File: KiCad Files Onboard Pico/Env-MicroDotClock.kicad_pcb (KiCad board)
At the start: 2 copper layers, 110 x 80 mm, 87 parts, among them IC1 IS31FL3730-QFLS2-TR, IC2 IS31FL3730-QFLS2-TR, IC3 IS31FL3730-QFLS2-TR, IC4 IS31FL3730-QFLS2-TR, J1 Conn_01x03, J3 Button, M1 Dip-14 Socket, M2 Dip-14 Socket, M3 Dip-14 Socket, M4 Dip-14 Socket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

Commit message: commit current progress
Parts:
- added R10: 0402 10K, Resistor_SMD:R_0402_1005Metric, F.Cu at (35.9, 61.1)
- added R11: 0402 10K, Resistor_SMD:R_0402_1005Metric, F.Cu at (35.9, 59.0)
- added R12: 0402 10K, Resistor_SMD:R_0402_1005Metric, F.Cu at (35.9, 60.0)
- added R13: 0402 10K, Resistor_SMD:R_0402_1005Metric, F.Cu at (35.9, 58.0)
- added R28: 0402 10K, Resistor_SMD:R_0402_1005Metric, F.Cu at (35.9, 57.0)
- added R5: 0402 10K, Resistor_SMD:R_0402_1005Metric, F.Cu at (35.9, 52.9)
- added R6: 0402 10K, Resistor_SMD:R_0402_1005Metric, F.Cu at (35.9, 54.0)
- added R7: 0402 10K, Resistor_SMD:R_0402_1005Metric, F.Cu at (35.9, 55.0)
- added R8: 0402 10K, Resistor_SMD:R_0402_1005Metric, F.Cu at (35.9, 56.0)
- added R9: 0402 10K, Resistor_SMD:R_0402_1005Metric, F.Cu at (35.9, 62.1)
- moved J1 2.00 mm to (52.0, 54.2), turned to 90 degrees
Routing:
- net +3V3: track 218.5 -> 129.0 mm, vias 8 -> 7
- net GPIO6: track 40.9 -> 84.5 mm, vias 2 -> 4
- net GPIO7: track 40.5 -> 82.2 mm, vias 0 -> 2
- net GPIO8: track 25.4 -> 66.0 mm, vias 2 -> 4
- net GPIO9: track 23.1 -> 62.6 mm, vias 0 -> 2
- net GPIO10: track 14.8 -> 52.6 mm, vias 0 -> 2
- net GPIO11: track 17.6 -> 54.2 mm, vias 0 -> 2
- net GPIO14: track 41.3 -> 74.1 mm, vias 2 -> 4
- net GPIO13: track 24.8 -> 56.6 mm, vias 0 -> 2
- net GPIO15: track 40.3 -> 71.9 mm, vias 0 -> 2
- net GPIO12: track 26.4 -> 57.3 mm, vias 2 -> 4
- net Net-(BT1-+): track 60.6 -> 50.3 mm
- net SWCLK: track 16.0 -> 11.8 mm
- net GND: vias 25 -> 22

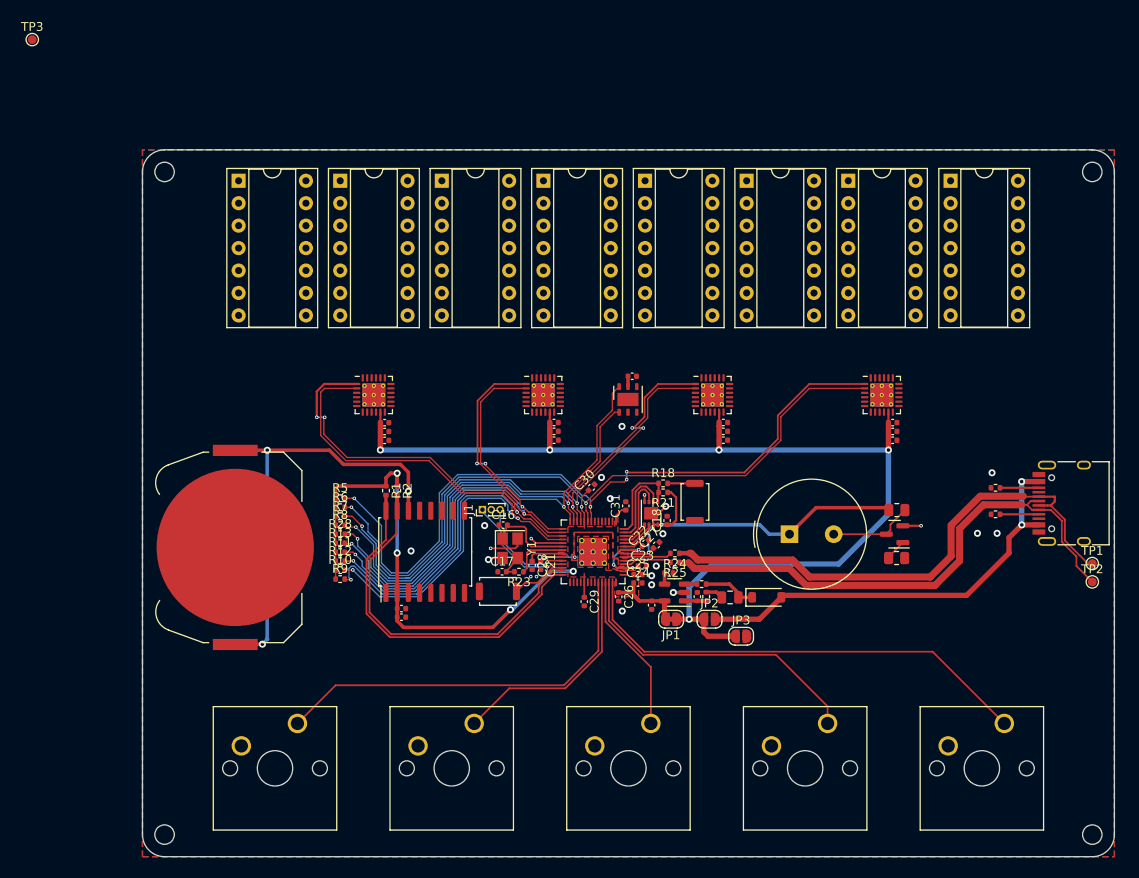
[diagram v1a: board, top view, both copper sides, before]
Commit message: finished up and cleaned up PCB, added logos
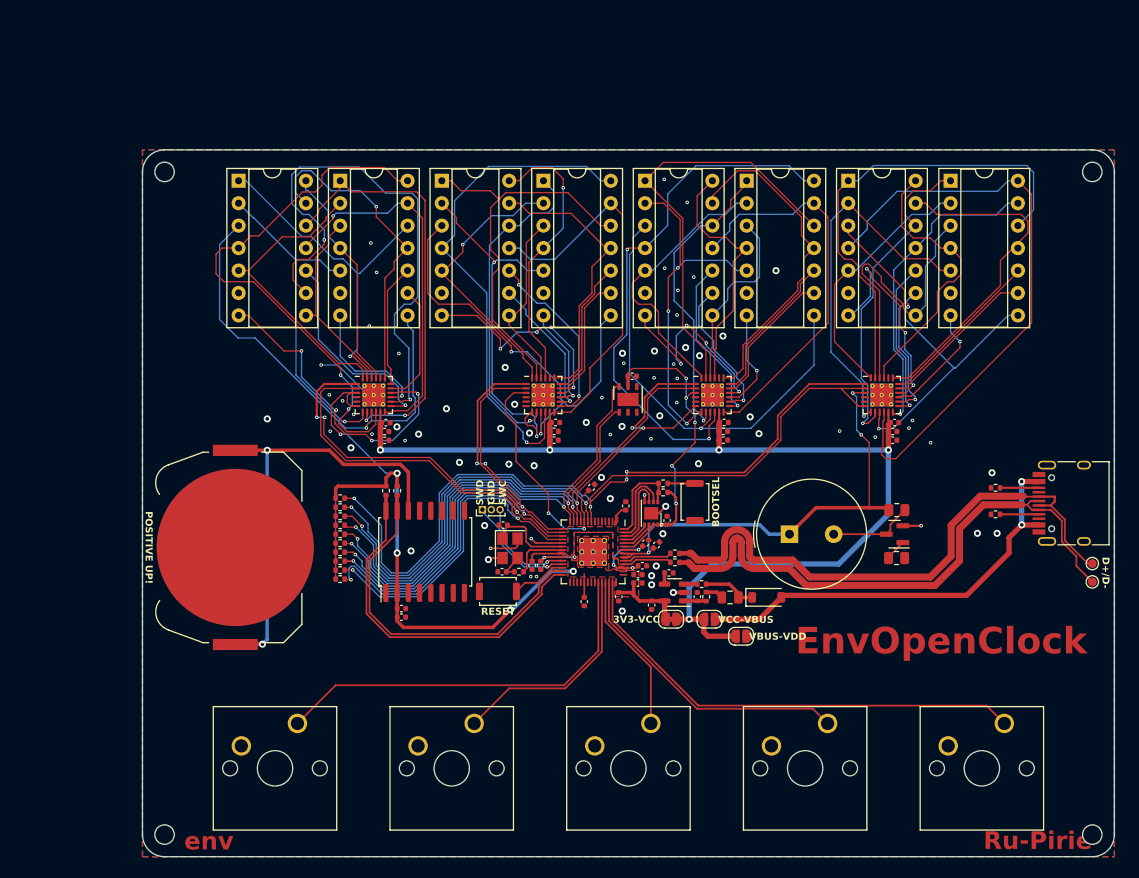
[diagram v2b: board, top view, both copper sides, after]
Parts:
- removed TP3: TestPoint, TestPoint:TestPoint_Pad_D1.0mm
- U2: value SOT-23-5 5.5V 3.3V 500mA -> TLV75733PDBVR
- moved C7 0.22 mm to (98.6, 44.4)
- moved C12 0.17 mm to (60.2, 44.4)
- moved C11 0.15 mm to (41.0, 44.4)
- moved C1 0.08 mm to (79.3, 44.4)
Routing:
- net +3V3: track 129.0 -> 208.2 mm, vias 7 -> 16
- net IC4R4: track 0.00 -> 68.0 mm
- net IC1R7: track 0.00 -> 61.5 mm, vias 0 -> 2
- net IC1R4: track 0.00 -> 61.5 mm, vias 0 -> 2
- net IC3R4: track 0.00 -> 60.1 mm, vias 0 -> 2
- net IC2R4: track 0.00 -> 57.2 mm, vias 0 -> 1
- net IC4C2: track 0.00 -> 53.7 mm
- net IC1R3: track 0.00 -> 53.0 mm, vias 0 -> 1
- net IC3R3: track 0.00 -> 51.8 mm, vias 0 -> 1
- net IC2R3: track 0.00 -> 50.6 mm, vias 0 -> 2
- net IC1R2: track 0.00 -> 48.3 mm, vias 0 -> 2
- net IC3C2: track 0.00 -> 48.1 mm
- net IC2C2: track 0.00 -> 45.2 mm
- net IC3R5: track 0.00 -> 44.3 mm
- net IC4R3: track 0.00 -> 44.2 mm, vias 0 -> 2
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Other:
- board text added: "3V3-VCC"
- board text added: "BOOTSEL"
- board text added: "D+/D-"
- board text added: "EnvOpenClock"
- board text added: "POSITIVE UP!"
- board text added: "RESET"
- board text added: "Ru-Pirie"
- board text added: "SWD GND SWC"
- board text added: "VBUS-VDD"
- board text added: "VCC-VBUS"
- board text added: "env"

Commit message: generated production files
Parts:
- added TP3: TestPoint, TestPoint:TestPoint_Pad_D1.0mm, F.Cu at (80.2, 52.0)
- H1, H2, H3, H4: value MountingHole -> M2
- J1: value Conn_01x03 -> 1mm 1x3
- SW1, SW2, SW3, SW4, SW5: value SW_Push -> MX Keyboard Switch
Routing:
- net /Onboard Pico/~{USB_BOOT}: track 3.09 -> 7.53 mm

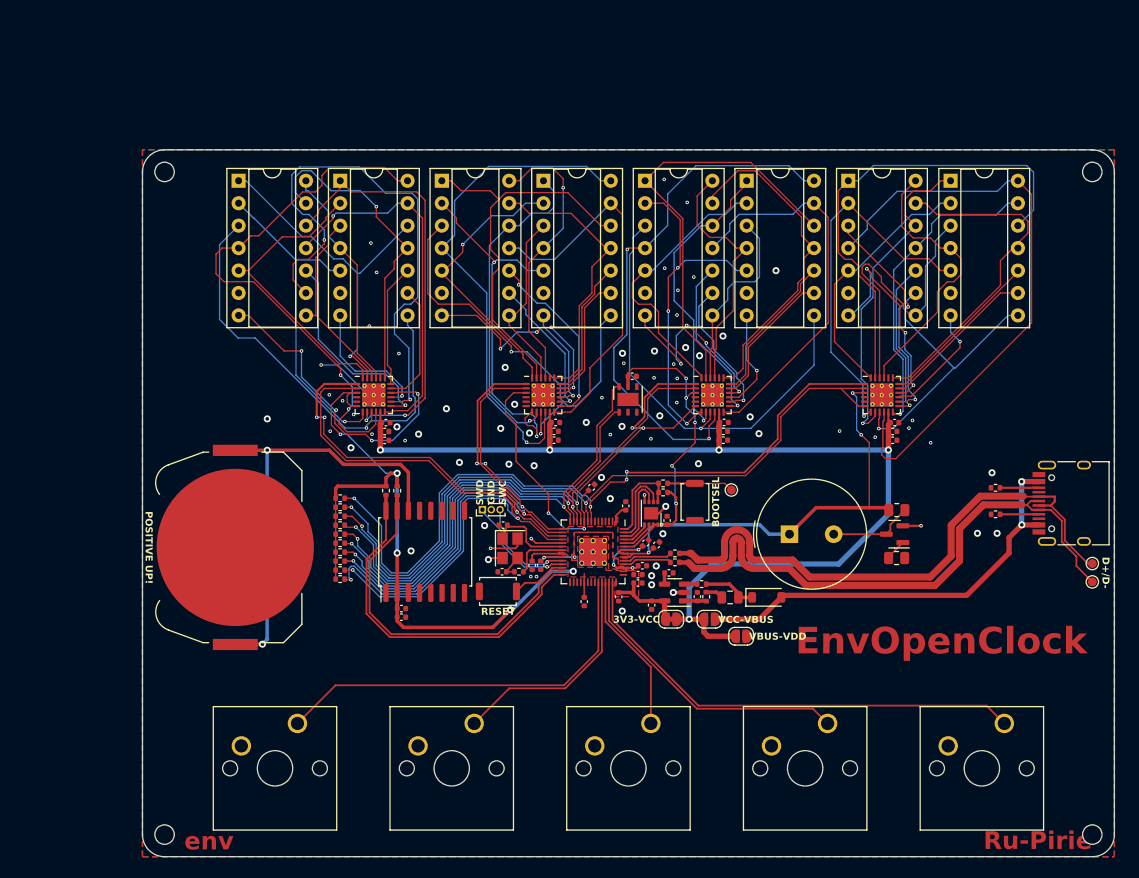
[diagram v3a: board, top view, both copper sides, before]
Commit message: added thermal vias, improved gnd connections from IS31FL37s, added thermal vias, added power only usb port on the back.
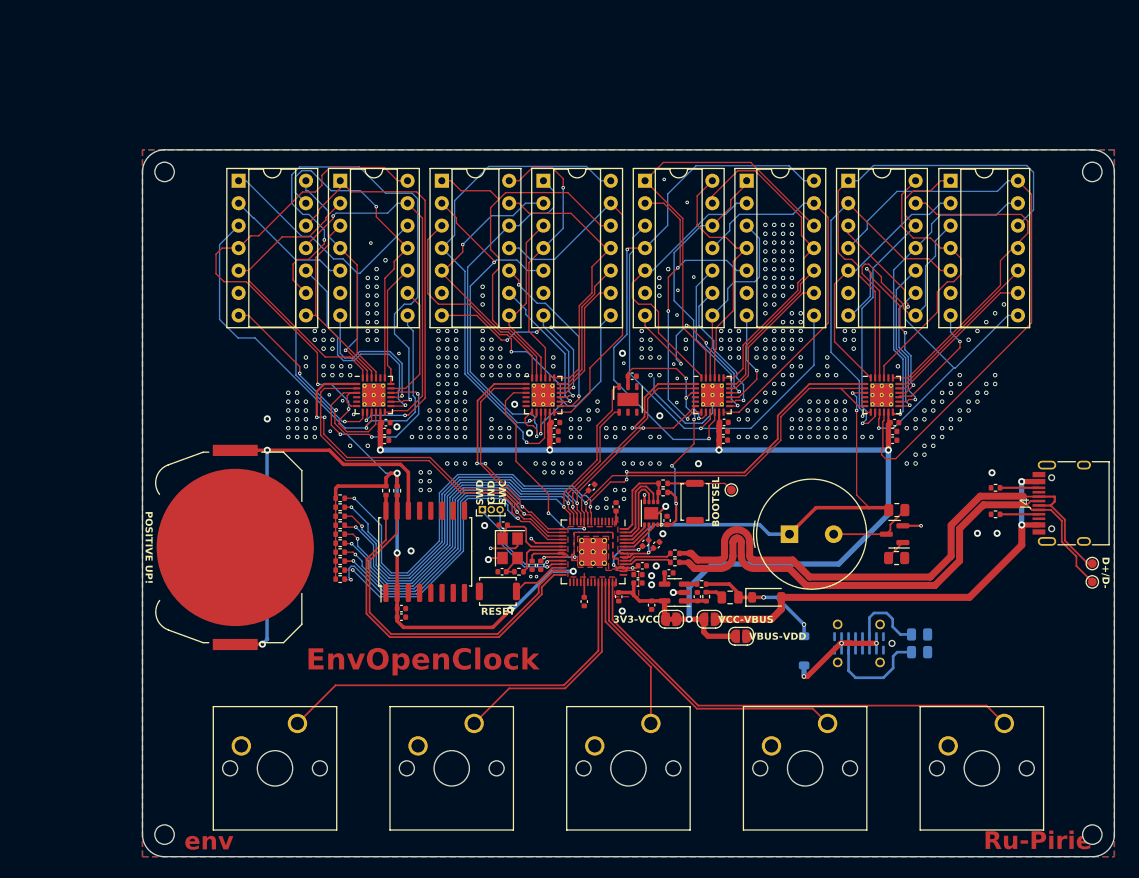
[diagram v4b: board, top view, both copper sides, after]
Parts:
- removed USB1: TYPE-C-31-M-12, Connector_USB:USB_C_Receptacle_HRO_TYPE-C-31-M-12
- added D2: 1N4002W, Diode_SMD:D_SOD-123, B.Cu at (88.4, 70.2)
- added J2: GT-USB-7051A, Connector_USB:USB_C_Receptacle_G-Switch_GT-USB-7051x, B.Cu at (94.6, 69.4)
- added J4: TYPE-C-31-M-12, Connector_USB:USB_C_Receptacle_HRO_TYPE-C-31-M-12, F.Cu at (119.0, 53.5)
- added R14: 5.1K 0805, Resistor_SMD:R_0805_2012Metric, B.Cu at (101.5, 68.3)
- added R17: 5.1K 0805, Resistor_SMD:R_0805_2012Metric, B.Cu at (101.5, 70.3)
- moved R15 3.00 mm to (110.0, 51.8)
- moved R16 3.00 mm to (110.0, 54.8)
- moved C31 1.10 mm to (67.1, 53.9)
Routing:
- net Net-(D2-A): track 0.00 -> 15.1 mm, vias 0 -> 3
- net Net-(J2-CC2): track 0.00 -> 11.8 mm
- net Net-(J2-CC1): track 0.00 -> 8.66 mm
- net VSYS: track 6.13 -> 14.6 mm, vias 0 -> 2
- net GND: track 24.4 -> 26.7 mm, vias 75 -> 423
- net IC2R2: track 36.9 -> 38.9 mm
- net IC2R1: track 42.8 -> 44.8 mm
- net IC1R6: track 23.8 -> 25.8 mm
- net IC1R8: track 15.4 -> 17.4 mm
- net IC1C8: track 35.8 -> 34.3 mm
- net IC2C8: track 25.2 -> 23.7 mm
- net VBUS: track 48.9 -> 50.0 mm
- net +3V3: track 208.2 -> 207.3 mm
- net IC3R1: track 40.1 -> 39.4 mm
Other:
- board text added: "PWR ONLY"

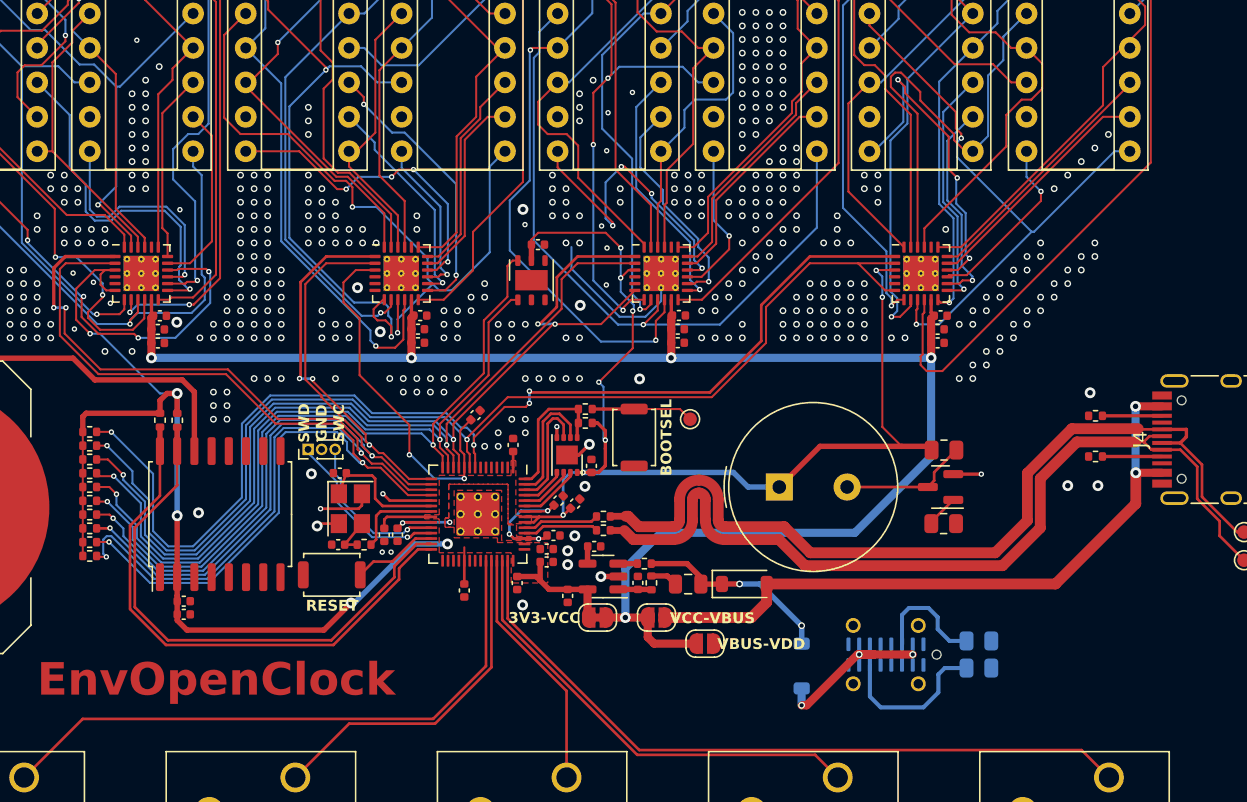
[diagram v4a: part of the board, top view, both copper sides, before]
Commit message: swapped LDO for more capable switching regulator.
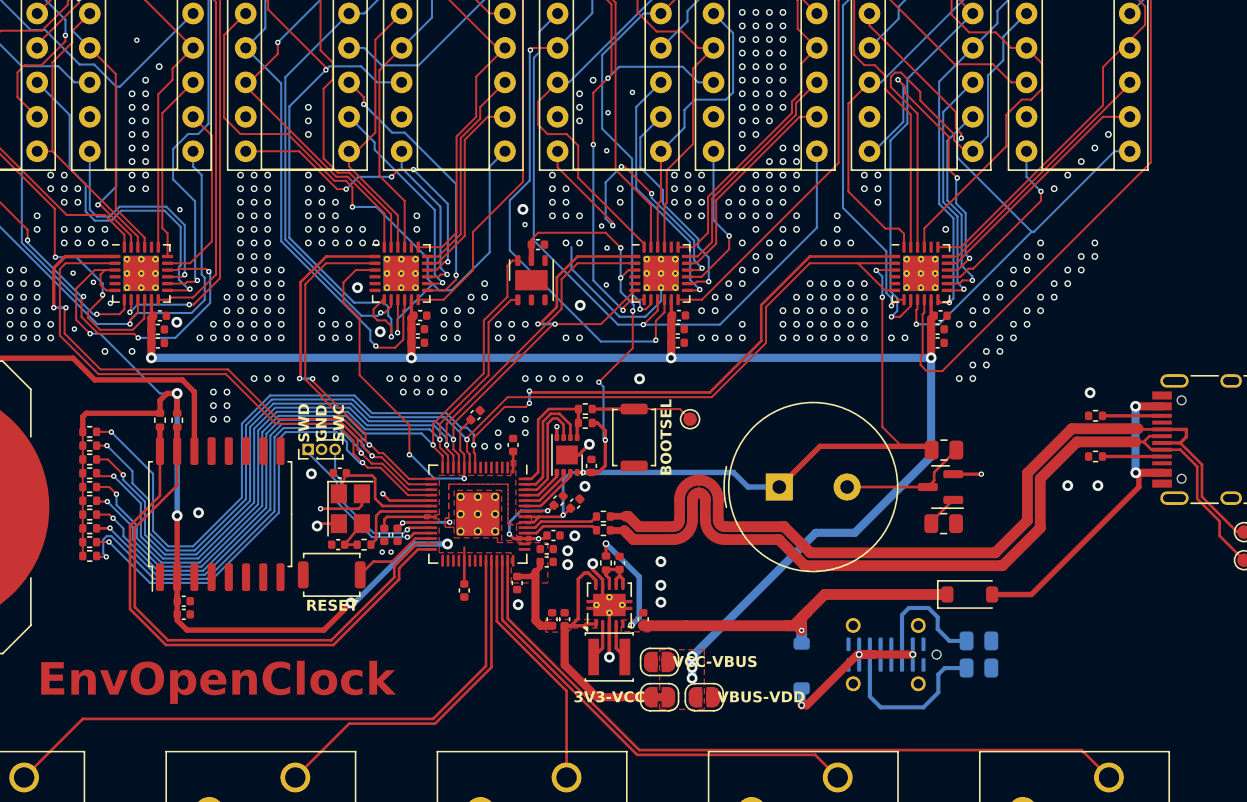
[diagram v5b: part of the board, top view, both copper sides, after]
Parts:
- removed CBP1: 10uf 0402, Capacitor_SMD:C_0402_1005Metric
- removed F1: 0805L050WR, Fuse:Fuse_0805_2012Metric
- removed FB1: FerriteBead 0402, Resistor_SMD:R_0402_1005Metric
- removed R22: 100K 0402, Resistor_SMD:R_0402_1005Metric
- added C15: 10uF 0402, Capacitor_SMD:C_0402_1005Metric, F.Cu at (76.7, 66.8)
- added C32: 10uF 0402, Capacitor_SMD:C_0402_1005Metric, F.Cu at (70.0, 66.8)
- added L1: SPH3015H2R2MT, Inductor_SMD:L_Sunlord_SWPA3015S, F.Cu at (74.2, 69.5)
- added R19: 100ohm 0402, Resistor_SMD:R_0402_1005Metric, F.Cu at (74.0, 62.6)
- C19: value 10uf 0402 -> 0.1uF 0402
- C20: value 10uf 0402 -> 10uF 0402
- D1, D2: value 1N4002W -> 1N5819W
- U2: value TLV75733PDBVR -> TPS63001DRCR; footprint Package_TO_SOT_SMD:SOT-23-5 -> Package_SON:Texas_DRC0010J_ThermalVias
- moved D1 16.6 mm to (100.8, 64.9)
- moved JP1 7.45 mm to (77.9, 72.5)
- moved JP3 3.95 mm to (81.2, 72.5)
- moved JP2 3.28 mm to (77.9, 69.9), turned to 180 degrees
- moved U2 2.15 mm to (74.2, 65.7), turned to 90 degrees
- moved C19 2.00 mm to (75.0, 62.6)
- moved C20 1.73 mm to (70.9, 66.8), turned to 90 degrees
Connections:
- C19 pad 1: Net-(U2-IN) -> Net-(U2-EN)
- D1 pad 2: VBUS -> Net-(D1-A)
- J4 pad A4: VBUS -> Net-(D1-A)
- J4 pad A9: VBUS -> Net-(D1-A)
- J4 pad B4: VBUS -> Net-(D1-A)
- J4 pad B9: VBUS -> Net-(D1-A)
- U2 pad 1: Net-(U2-IN) -> +3V3
- U2 pad 2: GND -> Net-(U2-L2)
- U2 pad 3: 3V3_EN -> GND
- U2 pad 5: +3V3 -> VSYS
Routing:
- net VBUS: track 50.0 -> 0.00 mm, vias 2 -> 0
- net Net-(D1-A): track 0.00 -> 24.0 mm, vias 0 -> 2
- net VSYS: track 14.6 -> 35.3 mm, vias 2 -> 3
- net +3V3: track 207.3 -> 224.2 mm
- net VCC: track 120.7 -> 108.2 mm, vias 5 -> 7
- net GND: track 26.7 -> 34.7 mm, vias 423 -> 427
- net Net-(U2-EN): track 0.00 -> 4.89 mm
- net Net-(U2-L2): track 0.00 -> 2.71 mm
- net Net-(U2-IN): track 2.45 -> 0.00 mm
- net Net-(F1-Pad1): track 2.02 -> 0.00 mm
- net Net-(U2-L1): track 1.28 -> 2.70 mm
- net 3V3_EN: track 1.41 -> 0.00 mm
- net IC4C1: track 29.2 -> 29.8 mm
- added copper zone on F.Cu, net VCC
- added copper zone on F.Cu, net VSYS
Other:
- board text added: "https://github.com/Envious-Data/EnvOpenClock"
